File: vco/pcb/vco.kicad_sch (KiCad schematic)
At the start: 40 parts

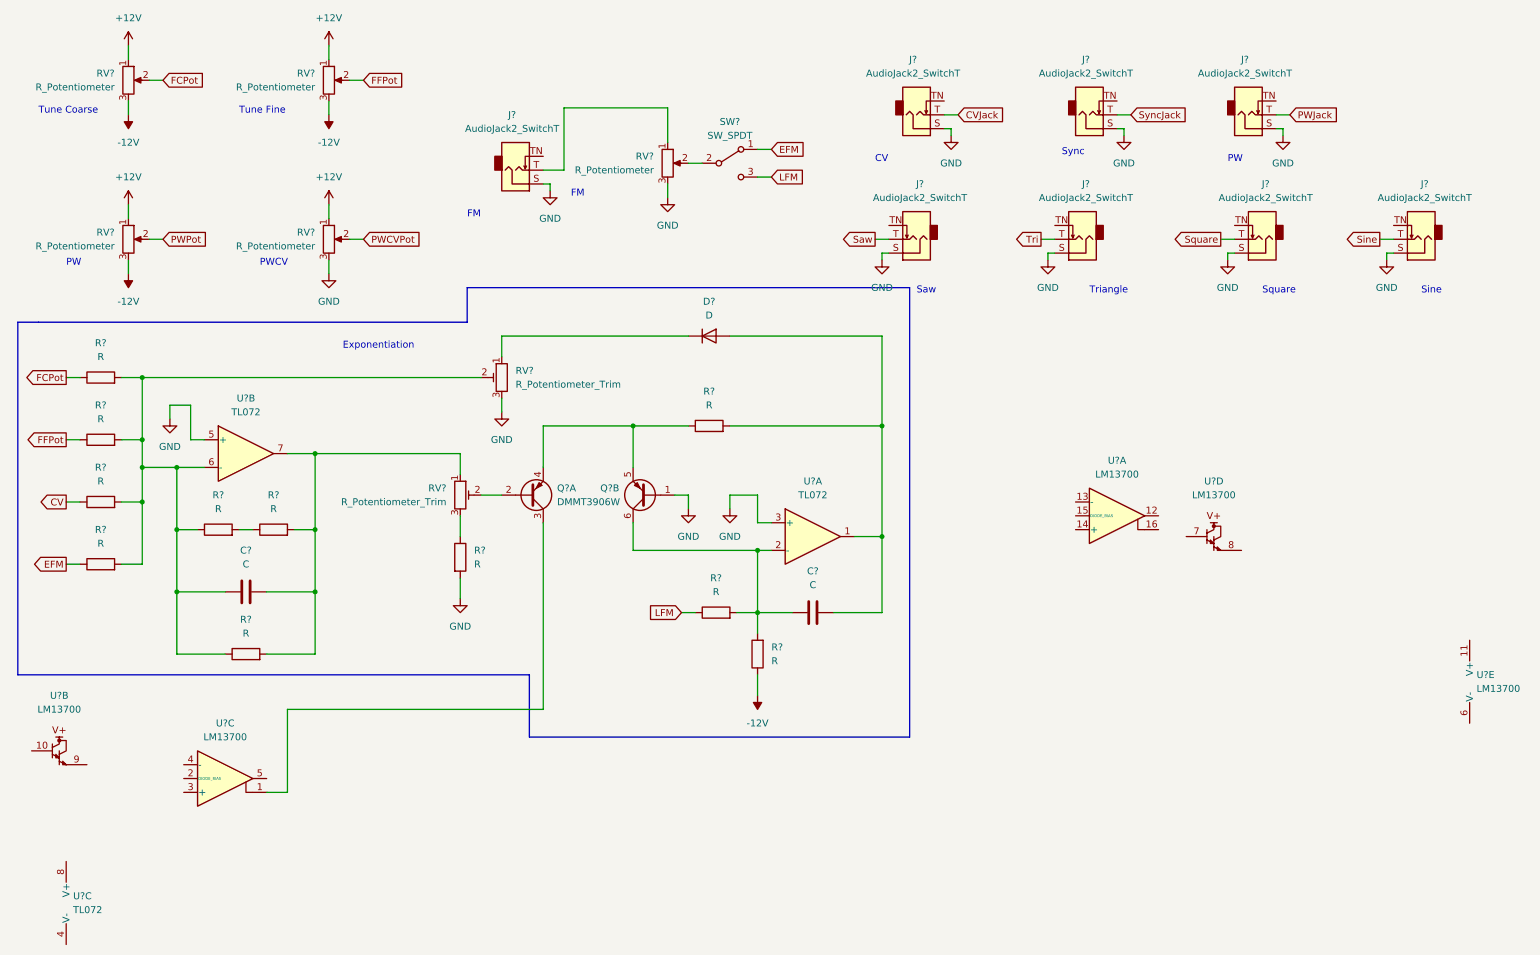
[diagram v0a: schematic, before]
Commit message: vco: Finish schematic
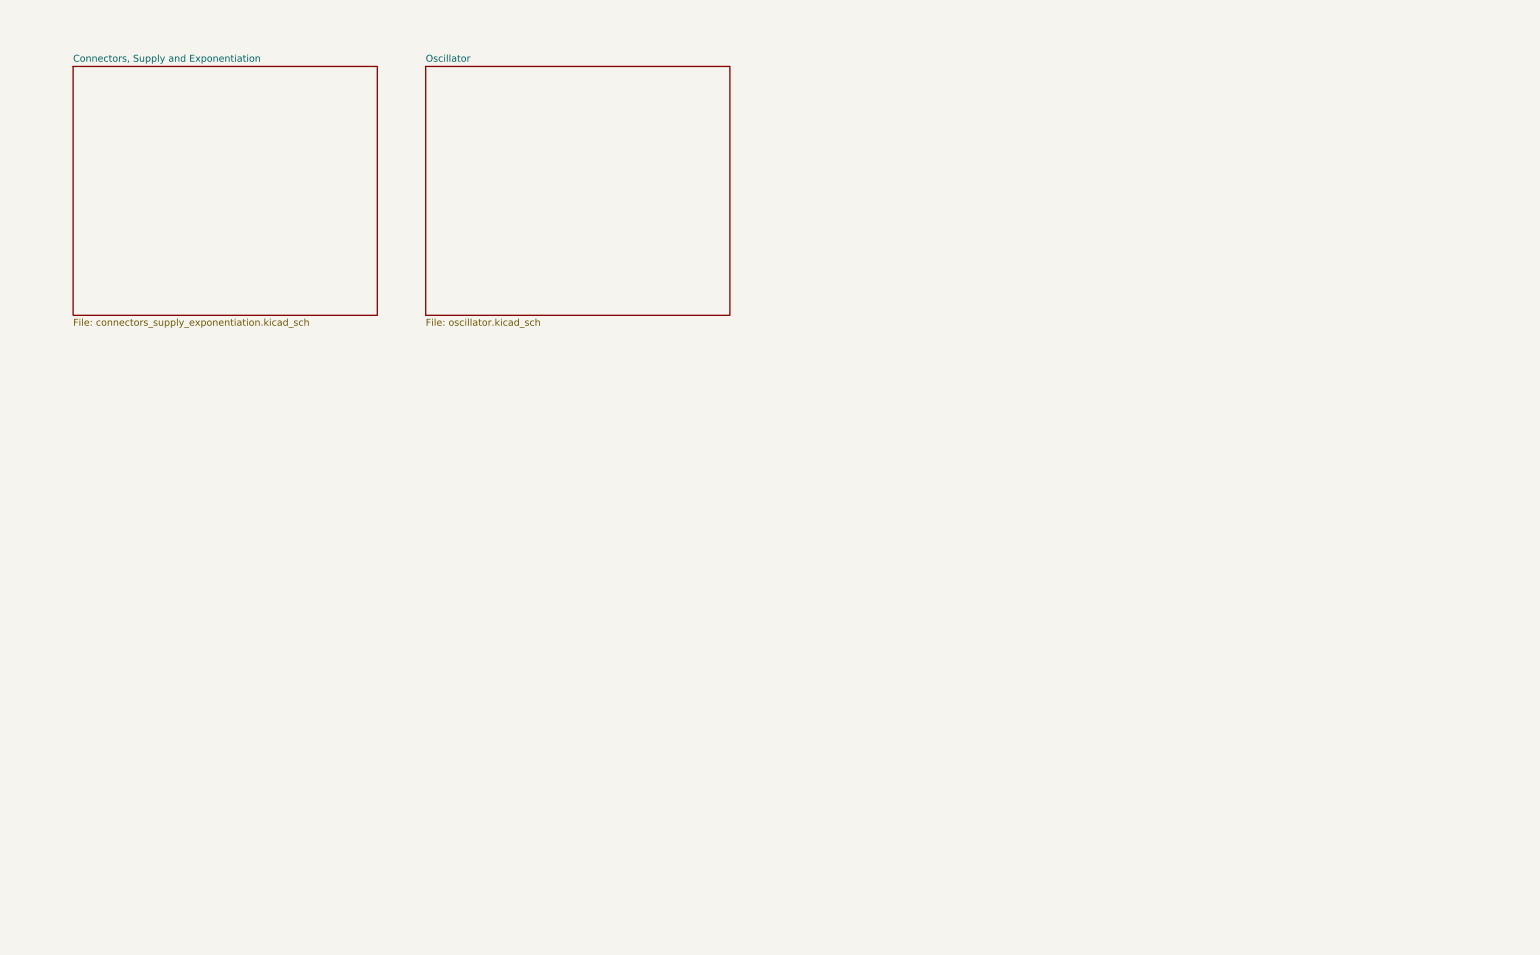
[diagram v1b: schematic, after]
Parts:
- removed C? (x2): C, symbol Device:C
- removed D?: D, symbol Device:D
- removed J? (x8): AudioJack2_SwitchT, symbol Connector:AudioJack2_SwitchT
- removed Q? (x2): DMMT3906W, Package_TO_SOT_SMD:SOT-363_SC-70-6, symbol My_Misc:DMMT3906W
- removed R? (x11): R, symbol Device:R
- removed RV? (x2): R_Potentiometer_Trim, symbol Device:R_Potentiometer_Trim
- removed RV? (x5): R_Potentiometer, symbol Device:R_Potentiometer
- removed SW?: SW_SPDT, symbol Switch:SW_SPDT
- removed U? (x5): LM13700, symbol Amplifier_Operational:LM13700
- removed U? (x3): TL072, symbol Amplifier_Operational:TL072
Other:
- added sheet Connectors, Supply and Exponentiation (connectors_supply_exponentiation.kicad_sch)
- added sheet Oscillator (oscillator.kicad_sch)
- note removed: "CV"
- note removed: "Exponentiation"
- note removed: "FM"
- note removed: "PW"
- note removed: "PWCV"
- note removed: "Saw"
- note removed: "Sine"
- note removed: "Square"
- note removed: "Sync"
- note removed: "Triangle"
- note removed: "Tune Coarse"
- note removed: "Tune Fine"
